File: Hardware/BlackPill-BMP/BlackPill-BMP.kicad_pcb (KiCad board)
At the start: 2 copper layers, 70 x 60 mm, 27 parts, among them J1 VCC, J2 VCC, J3 Conn_01x10, J4 Conn_01x11, J5 GDB_COMM, J6 VCC, J7 GND, J8 JTAG, J9 LogicAna, U1 STM32F411 BlackPill

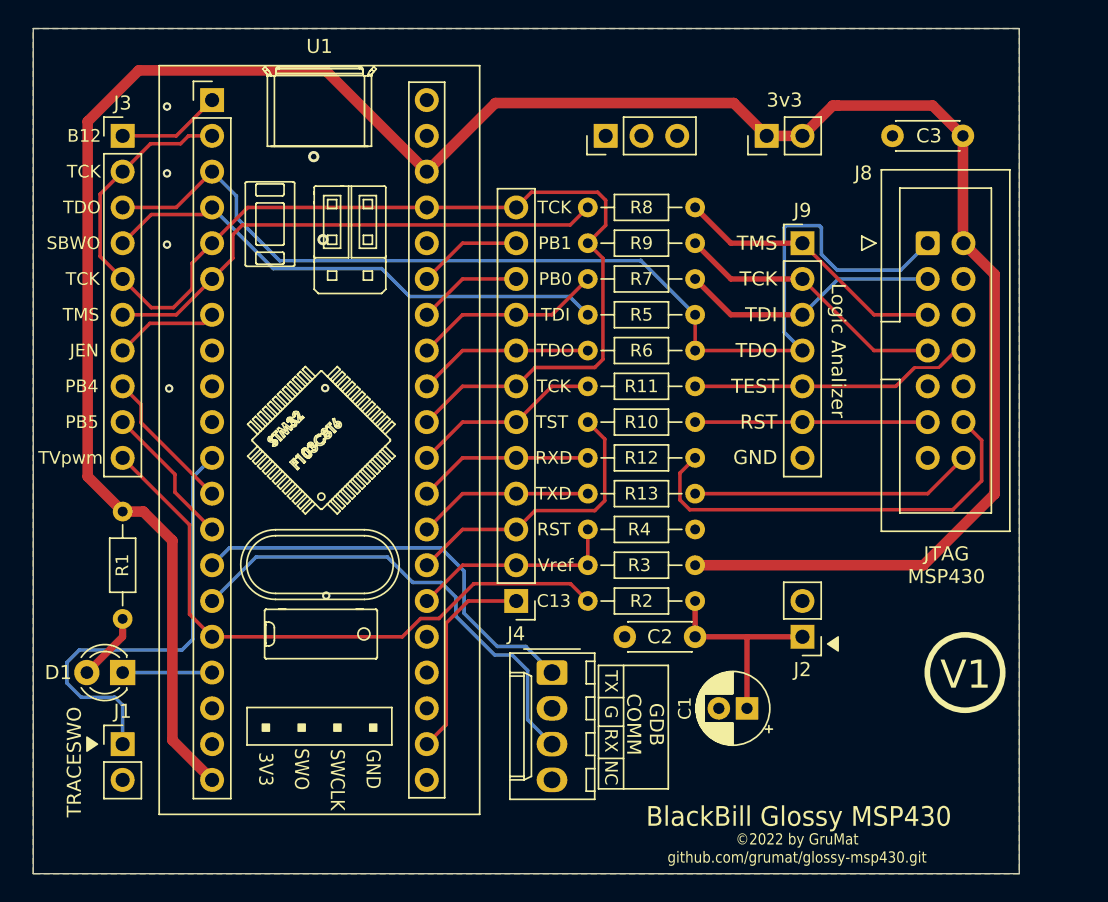
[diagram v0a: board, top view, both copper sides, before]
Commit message: Improved BlackPill Board to support both BluePill and BlackPill. Support for variable target voltage.
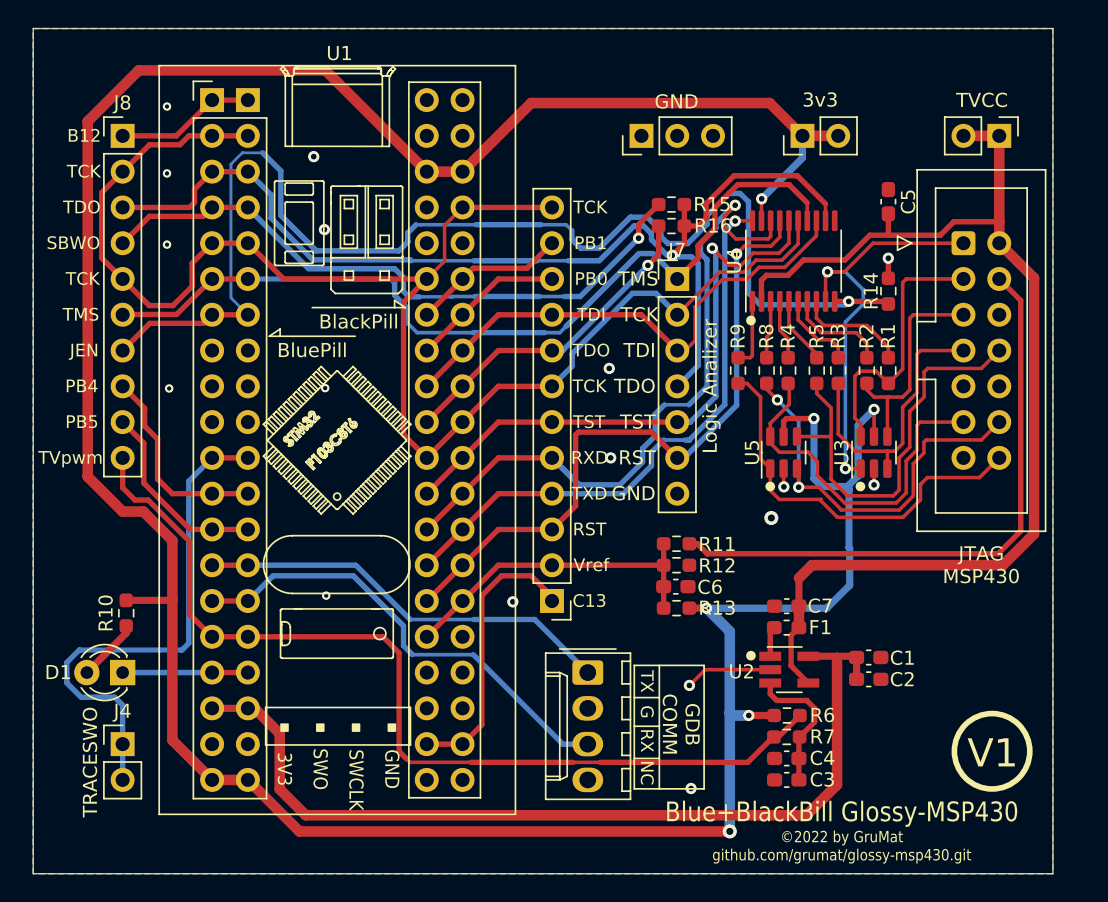
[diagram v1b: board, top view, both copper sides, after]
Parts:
- added C1: 100nF, Capacitor_SMD:C_0603_1608Metric_Pad1.08x0.95mm_HandSolder, F.Cu at (176.2, 109.7)
- added C2: 10uF, Capacitor_SMD:C_0603_1608Metric_Pad1.08x0.95mm_HandSolder, F.Cu at (176.2, 111.2)
- added C6: 100nF, Capacitor_SMD:C_0603_1608Metric_Pad1.08x0.95mm_HandSolder, F.Cu at (162.5, 104.6)
- added C7: 10uF, Capacitor_SMD:C_0603_1608Metric_Pad1.08x0.95mm_HandSolder, F.Cu at (170.3, 106.0)
- added F1: 0603L010YR, Fuse:Fuse_0603_1608Metric_Pad1.05x0.95mm_HandSolder, F.Cu at (170.3, 107.5)
- added R13: 470K, Resistor_SMD:R_0603_1608Metric_Pad0.98x0.95mm_HandSolder, F.Cu at (162.5, 106.1)
- added R14: 47K, Resistor_SMD:R_0603_1608Metric_Pad0.98x0.95mm_HandSolder, F.Cu at (177.5, 83.6)
- added R6: 47K, Resistor_SMD:R_0603_1608Metric_Pad0.98x0.95mm_HandSolder, F.Cu at (170.4, 113.8)
- added U2: AD8531ARTZ, Package_TO_SOT_SMD:SOT-23-5_HandSoldering, F.Cu at (170.5, 110.5)
- added U3: SRV05-4, Package_TO_SOT_SMD:SOT-23-6, F.Cu at (176.5, 95.1)
- added U4: TXS0108EPW, Package_SO:TSSOP-20_4.4x6.5mm_P0.65mm, F.Cu at (170.8, 81.5)
- added U5: SRV05-4, Package_TO_SOT_SMD:SOT-23-6, F.Cu at (170.1, 95.1)
- C3: renamed from C1; footprint Capacitor_THT:CP_Radial_D5.0mm_P2.00mm -> Capacitor_SMD:C_0603_1608Metric_Pad1.08x0.95mm_HandSolder
- C4: renamed from C2; footprint Capacitor_THT:C_Disc_D4.3mm_W1.9mm_P5.00mm -> Capacitor_SMD:C_0603_1608Metric_Pad1.08x0.95mm_HandSolder
- C5: renamed from C3; footprint Capacitor_THT:C_Disc_D4.3mm_W1.9mm_P5.00mm -> Capacitor_SMD:C_0603_1608Metric_Pad1.08x0.95mm_HandSolder
- J4: renamed from J1; value VCC -> SWO
- J6: renamed from J2; value VCC -> TVCC
- R1: renamed from R7; footprint Resistor_THT:R_Axial_DIN0204_L3.6mm_D1.6mm_P7.62mm_Horizontal -> Resistor_SMD:R_0603_1608Metric_Pad0.98x0.95mm_HandSolder
- R10: renamed from R1; footprint Resistor_THT:R_Axial_DIN0204_L3.6mm_D1.6mm_P7.62mm_Horizontal -> Resistor_SMD:R_0603_1608Metric_Pad0.98x0.95mm_HandSolder
- R11: renamed from R3; footprint Resistor_THT:R_Axial_DIN0204_L3.6mm_D1.6mm_P7.62mm_Horizontal -> Resistor_SMD:R_0603_1608Metric_Pad0.98x0.95mm_HandSolder
- R12: renamed from R4; footprint Resistor_THT:R_Axial_DIN0204_L3.6mm_D1.6mm_P7.62mm_Horizontal -> Resistor_SMD:R_0603_1608Metric_Pad0.98x0.95mm_HandSolder
- R15: renamed from R5; footprint Resistor_THT:R_Axial_DIN0204_L3.6mm_D1.6mm_P7.62mm_Horizontal -> Resistor_SMD:R_0603_1608Metric_Pad0.98x0.95mm_HandSolder
- R16: renamed from R6; footprint Resistor_THT:R_Axial_DIN0204_L3.6mm_D1.6mm_P7.62mm_Horizontal -> Resistor_SMD:R_0603_1608Metric_Pad0.98x0.95mm_HandSolder
- R2: renamed from R8; footprint Resistor_THT:R_Axial_DIN0204_L3.6mm_D1.6mm_P7.62mm_Horizontal -> Resistor_SMD:R_0603_1608Metric_Pad0.98x0.95mm_HandSolder
- R3: renamed from R9; footprint Resistor_THT:R_Axial_DIN0204_L3.6mm_D1.6mm_P7.62mm_Horizontal -> Resistor_SMD:R_0603_1608Metric_Pad0.98x0.95mm_HandSolder
- R4: renamed from R10; footprint Resistor_THT:R_Axial_DIN0204_L3.6mm_D1.6mm_P7.62mm_Horizontal -> Resistor_SMD:R_0603_1608Metric_Pad0.98x0.95mm_HandSolder
- R5: renamed from R11; footprint Resistor_THT:R_Axial_DIN0204_L3.6mm_D1.6mm_P7.62mm_Horizontal -> Resistor_SMD:R_0603_1608Metric_Pad0.98x0.95mm_HandSolder
- R7: renamed from R2; footprint Resistor_THT:R_Axial_DIN0204_L3.6mm_D1.6mm_P7.62mm_Horizontal -> Resistor_SMD:R_0603_1608Metric_Pad0.98x0.95mm_HandSolder
- R8: renamed from R12; value 330 -> 100; footprint Resistor_THT:R_Axial_DIN0204_L3.6mm_D1.6mm_P7.62mm_Horizontal -> Resistor_SMD:R_0603_1608Metric_Pad0.98x0.95mm_HandSolder
- R9: renamed from R13; value 330 -> 100; footprint Resistor_THT:R_Axial_DIN0204_L3.6mm_D1.6mm_P7.62mm_Horizontal -> Resistor_SMD:R_0603_1608Metric_Pad0.98x0.95mm_HandSolder
- U1: value STM32F411 BlackPill -> BlueAndBlackPill; footprint lib:BlackPill_F411 -> lib:BlueBlackPill
- moved J6 38.2 mm to (185.4, 72.6), turned to -90 degrees
- moved R2 16.8 mm to (176.0, 89.3), turned to 90 degrees
- moved R1 15.2 mm to (177.5, 89.3), turned to 90 degrees
- moved R8 14.1 mm to (168.9, 89.3), turned to -90 degrees
- moved R9 13.8 mm to (166.9, 89.3), turned to -90 degrees
- moved R3 13.6 mm to (174.0, 89.3), turned to 90 degrees
- moved R7 11.6 mm to (170.3, 115.3)
- moved C4 10.8 mm to (170.3, 116.8)
- moved J7 9.25 mm to (162.6, 82.8)
- moved R16 9.00 mm to (162.2, 79.0)
- moved R5 8.71 mm to (172.5, 89.3), turned to 90 degrees
- moved R15 8.00 mm to (162.2, 77.5)
- moved R4 7.55 mm to (170.4, 89.3), turned to 90 degrees
- moved C5 7.06 mm to (177.5, 77.3), turned to -90 degrees
- moved R11 6.48 mm to (162.5, 101.6)
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- renumbered J8 to J1, J6 to J2, J7 to J3, J9 to J7, J3 to J8, J4 to J9
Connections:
- C3 pad 1: /TVCC -> Net-(C3-Pad1)
- C4 pad 1: /TVCC -> Net-(C3-Pad1)
- C5 pad 1: +3V3 -> GND
- C5 pad 2: GND -> /TVCC
- J1 pad 2: +3V3 -> /TVCC
- J1 pad 4: unconnected-(J8-Pad4) -> /TVref
- J4 pad 2: GND -> /TRACESWO
- J6 pad 2: GND -> /TVCC
- J7 pad 1: /JTMS -> /mTMS
- J7 pad 2: /JTCK -> /mTCK
- J7 pad 3: /JTDI -> /mTDI
- J7 pad 4: /JTDO -> /LTDO
- J7 pad 5: /JTEST -> /mTEST
- J7 pad 6: /JRST -> /mRST
- J8 pad 3: /JTDO -> /LTDO
- R1 pad 2: /mTDI -> /LTDI
- R11 pad 2: +3V3 -> /TVref
- R15 pad 1: /JTDO -> /LTDO
- R16 pad 1: /JTDO -> /LTDO
- R2 pad 2: /mTMS -> /LTMS
- R3 pad 2: /mTCK -> /LTCK
- R4 pad 2: /mRST -> /LRST
- R5 pad 2: /mTEST -> /LTEST
- R7 pad 1: /TVCC -> Net-(C3-Pad1)
- R8 pad 1: /mRXD -> /LRXD
- R9 pad 1: /mTXD -> /LTXD
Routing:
- net /JENA: track 7.40 -> 87.1 mm, vias 0 -> 1
- net /LTDO: track 0.00 -> 75.8 mm, vias 0 -> 1
- net +5V: track 0.00 -> 64.9 mm
- net /TVCC: track 15.3 -> 79.6 mm
- net /JTDO: track 79.7 -> 30.0 mm, vias 0 -> 2
- net +3V3: track 172.3 -> 218.2 mm, vias 0 -> 6
- net /TVref: track 0.00 -> 43.0 mm
- net /mRXD: track 12.5 -> 50.8 mm, vias 0 -> 1
- net /mTMS: track 37.2 -> 68.8 mm
- net /mTEST: track 13.5 -> 42.2 mm, vias 0 -> 1
- net /mTXD: track 12.5 -> 41.0 mm, vias 0 -> 1
- net /mRST: track 20.6 -> 47.7 mm, vias 0 -> 1
- net /mTCK: track 82.8 -> 107.6 mm
- net /mTDI: track 13.5 -> 36.7 mm
- net /TV_PWM: track 44.1 -> 66.8 mm
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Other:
- board size 70 x 60 mm -> 72.4 x 60 mm
- board text added: "Blue+BlackBill Glossy-MSP430"
- board text removed: "BlackBill Glossy MSP430"
- board text removed: "TEST"

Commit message: Improvements on the ESD circuit.
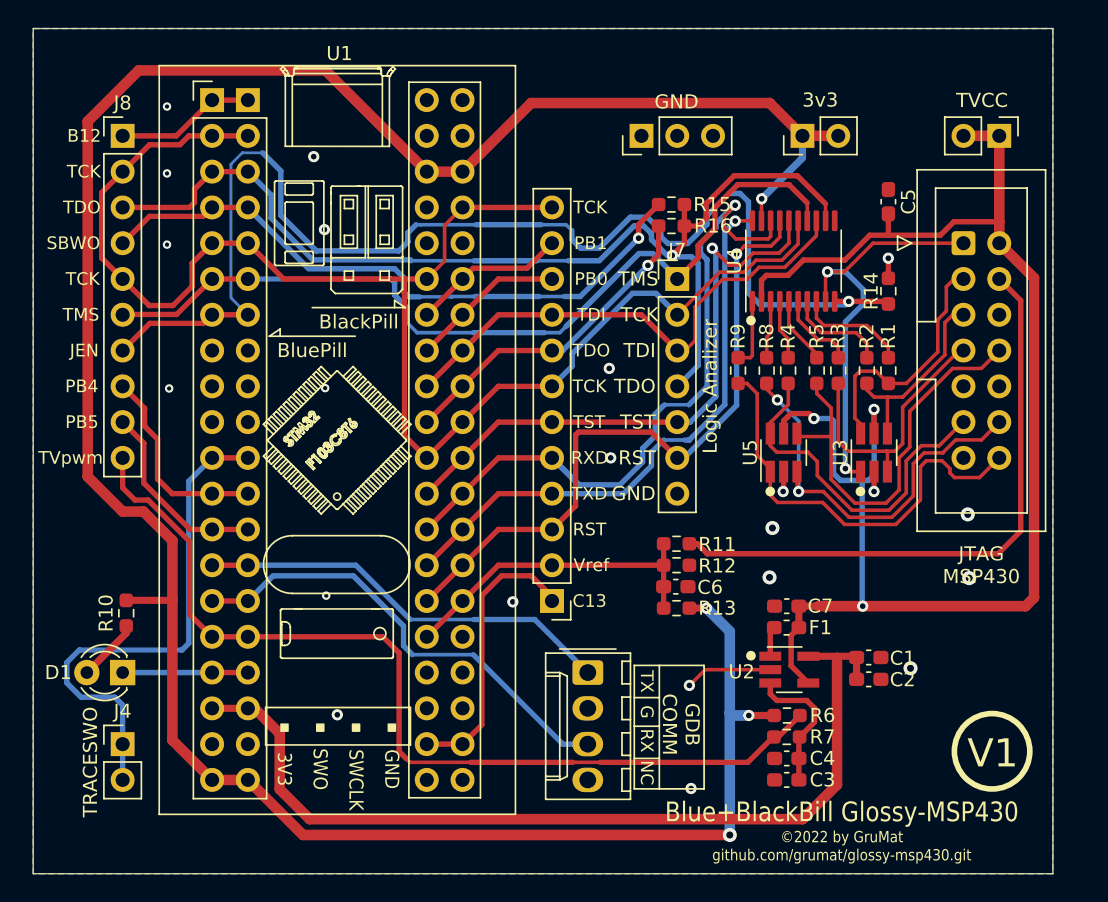
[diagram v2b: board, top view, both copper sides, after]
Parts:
- U3, U5: footprint Package_TO_SOT_SMD:SOT-23-6 -> Package_TO_SOT_SMD:SOT-23-6_Handsoldering
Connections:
- U3 pad 5: +3V3 -> /TVCC
- U5 pad 5: +3V3 -> /TVCC
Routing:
- net +3V3: track 218.2 -> 182.2 mm, vias 6 -> 4
- net /TVCC: track 79.6 -> 108.3 mm, vias 0 -> 3
- net /JRXD: track 28.4 -> 30.9 mm
- net /JTMS: track 15.8 -> 13.9 mm
- net /JTDI: track 19.3 -> 17.9 mm
- net /JTCK: track 20.3 -> 19.3 mm
- net /mTCK: track 107.6 -> 106.9 mm
- net /JTEST: track 30.2 -> 29.6 mm
- net /JRST: track 25.6 -> 25.1 mm
- net GND: track 10.1 -> 10.5 mm, vias 17 -> 22

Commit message: Variable voltage level for the L432KC board. Minor fixes on the Blue+Blackpill board.
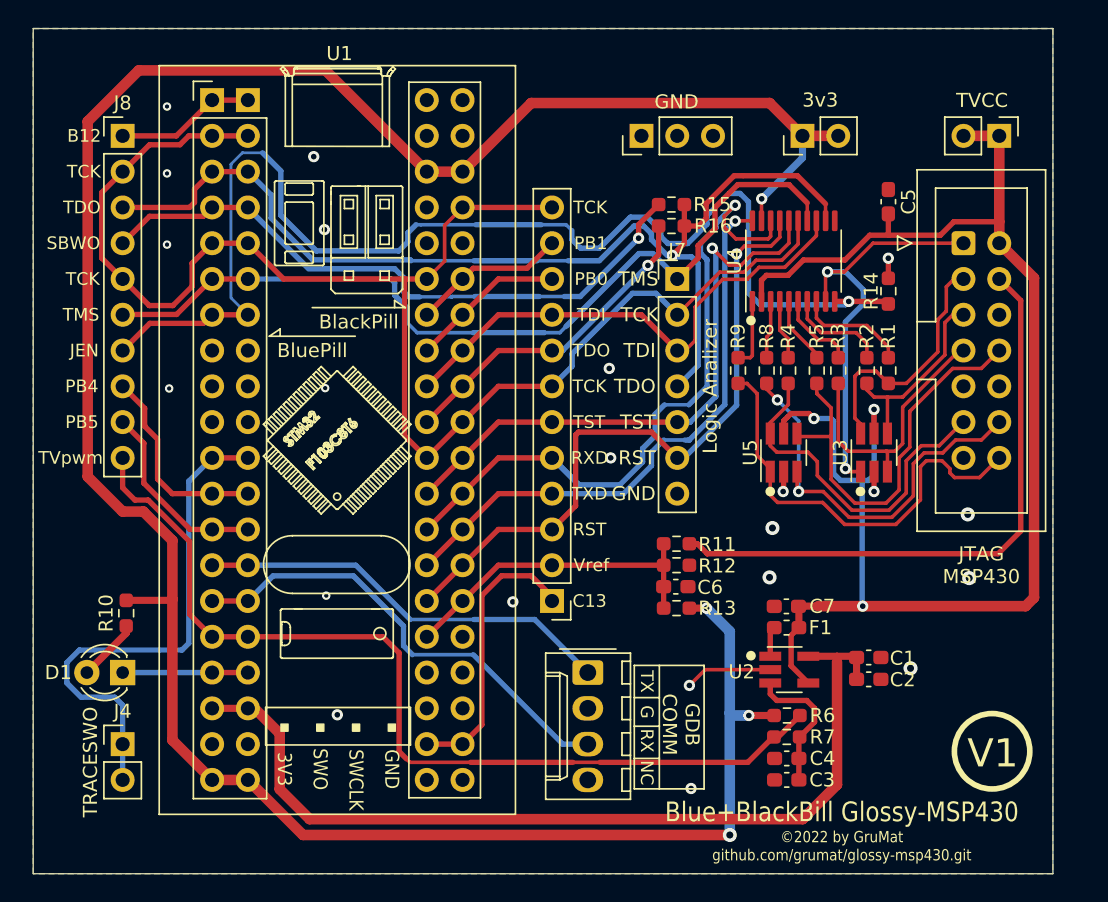
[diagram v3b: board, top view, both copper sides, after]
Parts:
- R16: value 100 -> 22
- turned C7 to 0 degrees
- turned C3 to 0 degrees
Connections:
- C3 pad 1: Net-(C3-Pad1) -> GND
- C3 pad 2: GND -> Net-(C3-Pad2)
- C4 pad 1: Net-(C3-Pad1) -> Net-(C3-Pad2)
- C7 pad 1: /TVCC -> GND
- C7 pad 2: GND -> /TVCC
- R7 pad 1: Net-(C3-Pad1) -> Net-(C3-Pad2)
- U2 pad 3: Net-(C3-Pad1) -> Net-(C3-Pad2)
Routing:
- net Net-(C3-Pad2): track 0.00 -> 9.89 mm
- net Net-(C3-Pad1): track 9.89 -> 0.00 mm

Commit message: Improved JTAG bus impedance for BlackPill. Various enhancements for Nucleo K432KC. Added SpiBiWire Adapter.
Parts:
- R1, R2, R3: value 100 -> 47
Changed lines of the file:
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@@
       (effects (font (size 1 1) (thickness 0.15)))
     )
-    (fp_text value "100" (at 0 1.43 90) (layer "F.Fab")
+    (fp_text value "47" (at 0 1.43 90) (layer "F.Fab")
       (effects (font (size 1 1) (thickness 0.15)))
     )
@@
       (effects (font (size 1 1) (thickness 0.15)))
     )
-    (fp_text value "100" (at 0 1.43 90) (layer "F.Fab")
+    (fp_text value "47" (at 0 1.43 90) (layer "F.Fab")
       (effects (font (size 1 1) (thickness 0.15)))
     )
@@
       (effects (font (size 1 1) (thickness 0.15)))
     )
-    (fp_text value "100" (at 0 1.43 90) (layer "F.Fab")
+    (fp_text value "47" (at 0 1.43 90) (layer "F.Fab")
       (effects (font (size 1 1) (thickness 0.15)))
     )
@@
     (fp_arc (start 9.164109 23.475359) (mid 9.19312 23.534447) (end 9.169421 23.59583) (layer "F.SilkS") (width 0.12))
     (fp_arc (start 7.057769 23.137421) (mid 6.881082 23.21257) (end 6.704534 23.137103) (layer "F.SilkS") (width 0.12))
-    (fp_arc (start 5.238052 24.032461) (mid 5.300527 24.004423) (end 5.368722 24.010576) (layer "F.SilkS") (width 0.12))
+    (fp_arc (start 5.238052 24.032461) (mid 5.300519 24.004429) (end 5.368722 24.010576) (layer "F.SilkS") (width 0.12))
     (fp_arc (start 6.919342 22.160794) (mid 7.078414 22.093934) (end 7.23752 22.160688) (layer "F.SilkS") (width 0.12))
     (fp_arc (start 5.698 35.022588) (mid 3.648 32.972588) (end 5.698 30.922588) (layer "F.SilkS") (width 0.12))
@@
     (fp_arc (start 4.534 11.742) (mid 4.463289 11.712711) (end 4.434 11.642) (layer "F.SilkS") (width 0.12))
     (fp_arc (start 5.153056 37.032958) (mid 5.435907 37.150103) (end 5.553056 37.432958) (layer "F.SilkS") (width 0.12))
-    (fp_arc (start 5.139252 24.209874) (mid 5.0841 24.072059) (end 5.143927 23.93621) (layer "F.SilkS") (width 0.12))
+    (fp_arc (start 5.139252 24.209874) (mid 5.084094 24.072059) (end 5.143927 23.93621) (layer "F.SilkS") (width 0.12))
     (fp_arc (start 9.317515 23.529327) (mid 9.430619 23.534642) (end 9.527224 23.593706) (layer "F.SilkS") (width 0.12))
     (fp_arc (start 5.459023 24.262355) (mid 5.542039 24.256717) (end 5.62082 24.283496) (layer "F.SilkS") (width 0.12))
-    (fp_arc (start 8.952381 23.377727) (mid 9.10311 23.311267) (end 9.254729 23.375603) (layer "F.SilkS") (width 0.12))
+    (fp_arc (start 8.952381 23.377727) (mid 9.10311 23.311203) (end 9.254729 23.375603) (layer "F.SilkS") (width 0.12))
     (fp_arc (start 11.765 -2.226605) (mid 11.931822 -2.175277) (end 12.014999 -2.021817) (layer "F.SilkS") (width 0.12))
     (fp_arc (start 5.284 6.742) (mid 5.213289 6.712711) (end 5.184 6.642) (layer "F.SilkS") (width 0.12))
@@
     (fp_arc (start 8.035776 25.146132) (mid 8.038453 25.196504) (end 8.014105 25.240682) (layer "F.SilkS") (width 0.12))
     (fp_arc (start 10.130326 23.124461) (mid 10.057435 23.149835) (end 9.98797 23.116175) (layer "F.SilkS") (width 0.12))
-    (fp_arc (start 4.96647 38.715042) (mid 4.943904 38.616315) (end 4.944082 38.515042) (layer "F.SilkS") (width 0.12))
+    (fp_arc (start 4.96647 38.715042) (mid 4.943912 38.616314) (end 4.944082 38.515042) (layer "F.SilkS") (width 0.12))
     (fp_arc (start 5.131166 -1.890847) (mid 5.176978 -1.815287) (end 5.193572 -1.7285) (layer "F.SilkS") (width 0.12))
     (fp_arc (start 8.519575 24.925586) (mid 8.342887 25.00072) (end 8.166341 24.925267) (layer "F.SilkS") (width 0.12))
@@
     (fp_arc (start 7.23752 22.160688) (mid 7.328273 22.324575) (end 7.354273 22.510098) (layer "F.SilkS") (width 0.12))
     (fp_arc (start 12.859998 39.524619) (mid 12.830711 39.594711) (end 12.760619 39.623998) (layer "F.SilkS") (width 0.12))
-    (fp_arc (start 5.315142 -2.054759) (mid 5.407725 -1.90088) (end 5.439988 -1.724215) (layer "F.SilkS") (width 0.12))
+    (fp_arc (start 5.315142 -2.054759) (mid 5.407732 -1.900877) (end 5.439988 -1.724215) (layer "F.SilkS") (width 0.12))
     (fp_arc (start 8.441283 6.21) (mid 8.470571 6.139283) (end 8.541283 6.11) (layer "F.SilkS") (width 0.12))
     (fp_arc (start 9.265884 23.689744) (mid 9.344175 23.652102) (end 9.425556 23.682413) (layer "F.SilkS") (width 0.12))
